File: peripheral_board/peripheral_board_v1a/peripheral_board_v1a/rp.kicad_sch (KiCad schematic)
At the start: 63 parts, among them CN1 Power Board Connector, CN2 DF11-16DP-2DSA(08), J1 Conn_01x03_Pin, J2 Conn_01x06, J3 Conn_02x06_Odd_Even, J4 Conn_01x06, J5 USB_C_Receptacle_USB2.0_16P, SW1 EVPAA602W, SW2 EVPAA602W, U1 RP2350A_C42411118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

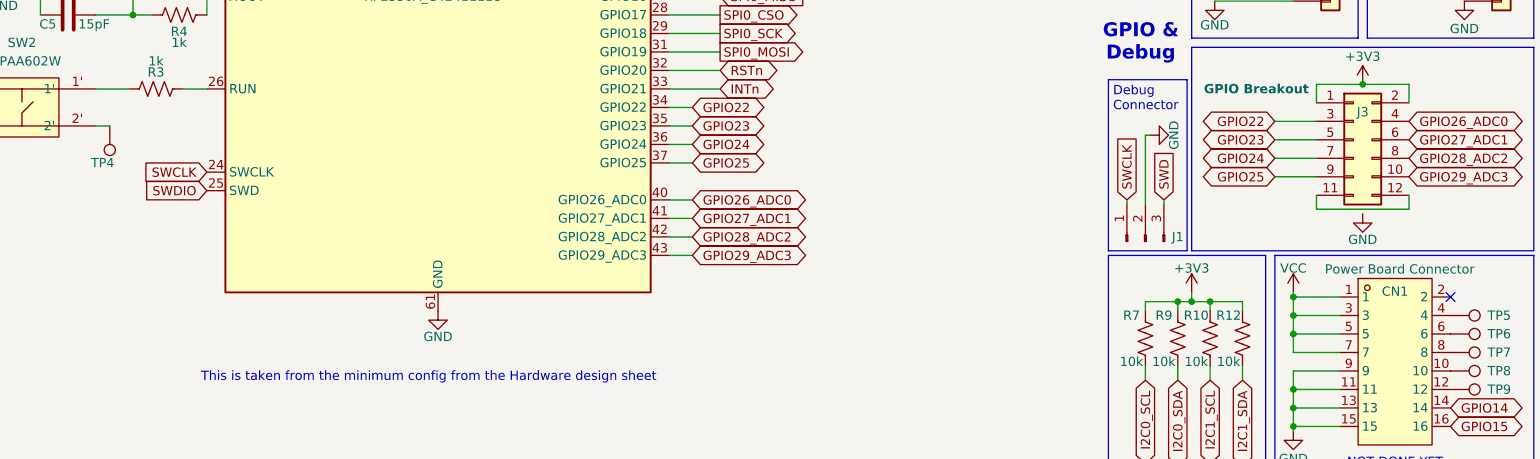
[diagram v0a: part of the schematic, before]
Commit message: PCB Update
Got all the parts on the board placed. Now just finishing the routing for each interconnection.
Trying to maintain a side to side/up to down but the board kinda follows it. For each plane  there is fill zones that will be for the chip that is on the top. Some of the traces are just being fed to where they need to go but the important EMI signals are being contained to their guidelines.
I will need to look at the lengths of the traces to make sure they are kept around the same length.

Will need to go over the board with some other eyes to make sure its ok.

I made sure the Wiznet traces are the same as SALAD.
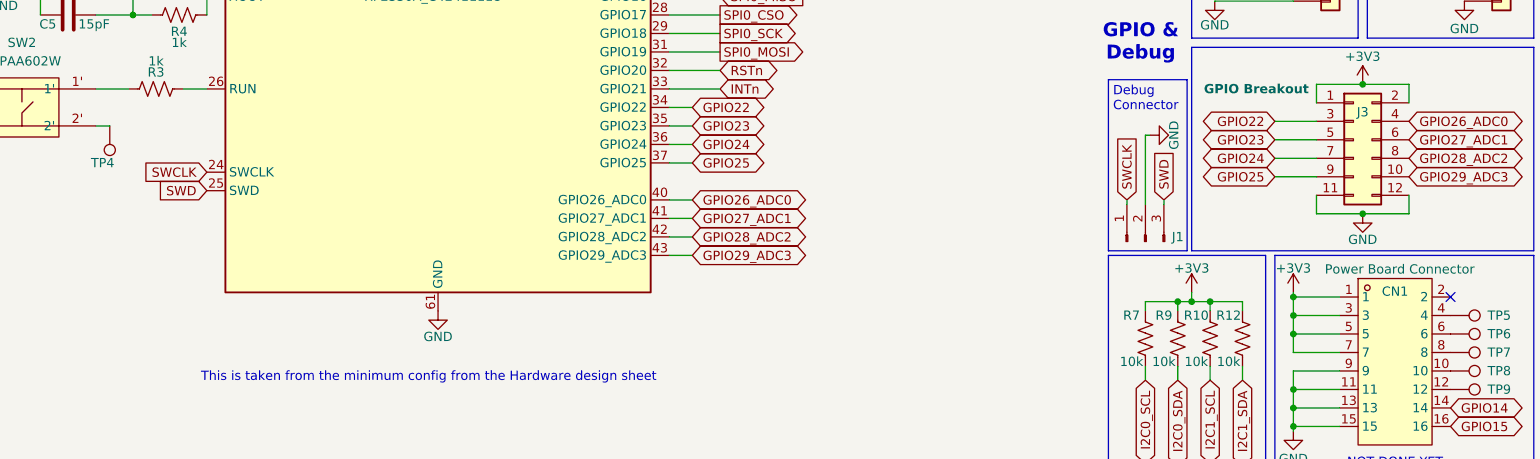
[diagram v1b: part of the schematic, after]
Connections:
- net SWDIO is gone; now on net SWD: U1.25 (SWD)
- net VCC is gone; now on net +3V3: CN1.1, CN1.3, CN1.5, CN1.7
- net GND: now also J3.11 (Pin_11), J3.12 (Pin_12)
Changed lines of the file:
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@@
 	)
 	(junction
+		(at 212.09 128.905)
+		(diameter 0)
+		(color 0 0 0 0)
+	)
+	(junction
 		(at 118.11 34.29)
 		(diameter 0)
@@
 	(wire
 		(pts
-			(xy 205.74 128.27) (xy 218.44 128.27)
+			(xy 205.74 128.905) (xy 212.09 128.905)
 		)
 		(stroke
@@
 	(wire
 		(pts
-			(xy 218.44 128.27) (xy 218.44 126.365)
+			(xy 218.44 128.905) (xy 218.44 126.365)
 		)
 		(stroke
@@
 	(wire
 		(pts
-			(xy 205.74 126.365) (xy 205.74 128.27)
+			(xy 205.74 126.365) (xy 205.74 128.905)
 		)
 		(stroke
@@
 	(wire
 		(pts
+			(xy 212.09 128.905) (xy 218.44 128.905)
+		)
+		(stroke
+			(width 0)
+			(type default)
+		)
+	)
+	(wire
+		(pts
 			(xy 123.19 76.2) (xy 116.84 76.2)
 		)
@@
 		)
 	)
-	(global_label "SWDIO"
+	(global_label "SWD"
 		(shape input)
 		(at 53.34 125.73 180)
@@
 		)
 		(property "Intersheetrefs" "${INTERSHEET_REFS}"
-			(at 44.4886 125.73 0)
+			(at 46.4239 125.73 0)
 			(effects
 				(font
@@
 			)
 		)
-		(property "Value" "VCC"
+		(property "Value" "+3V3"
 			(at 202.565 136.398 0)
 			(effects

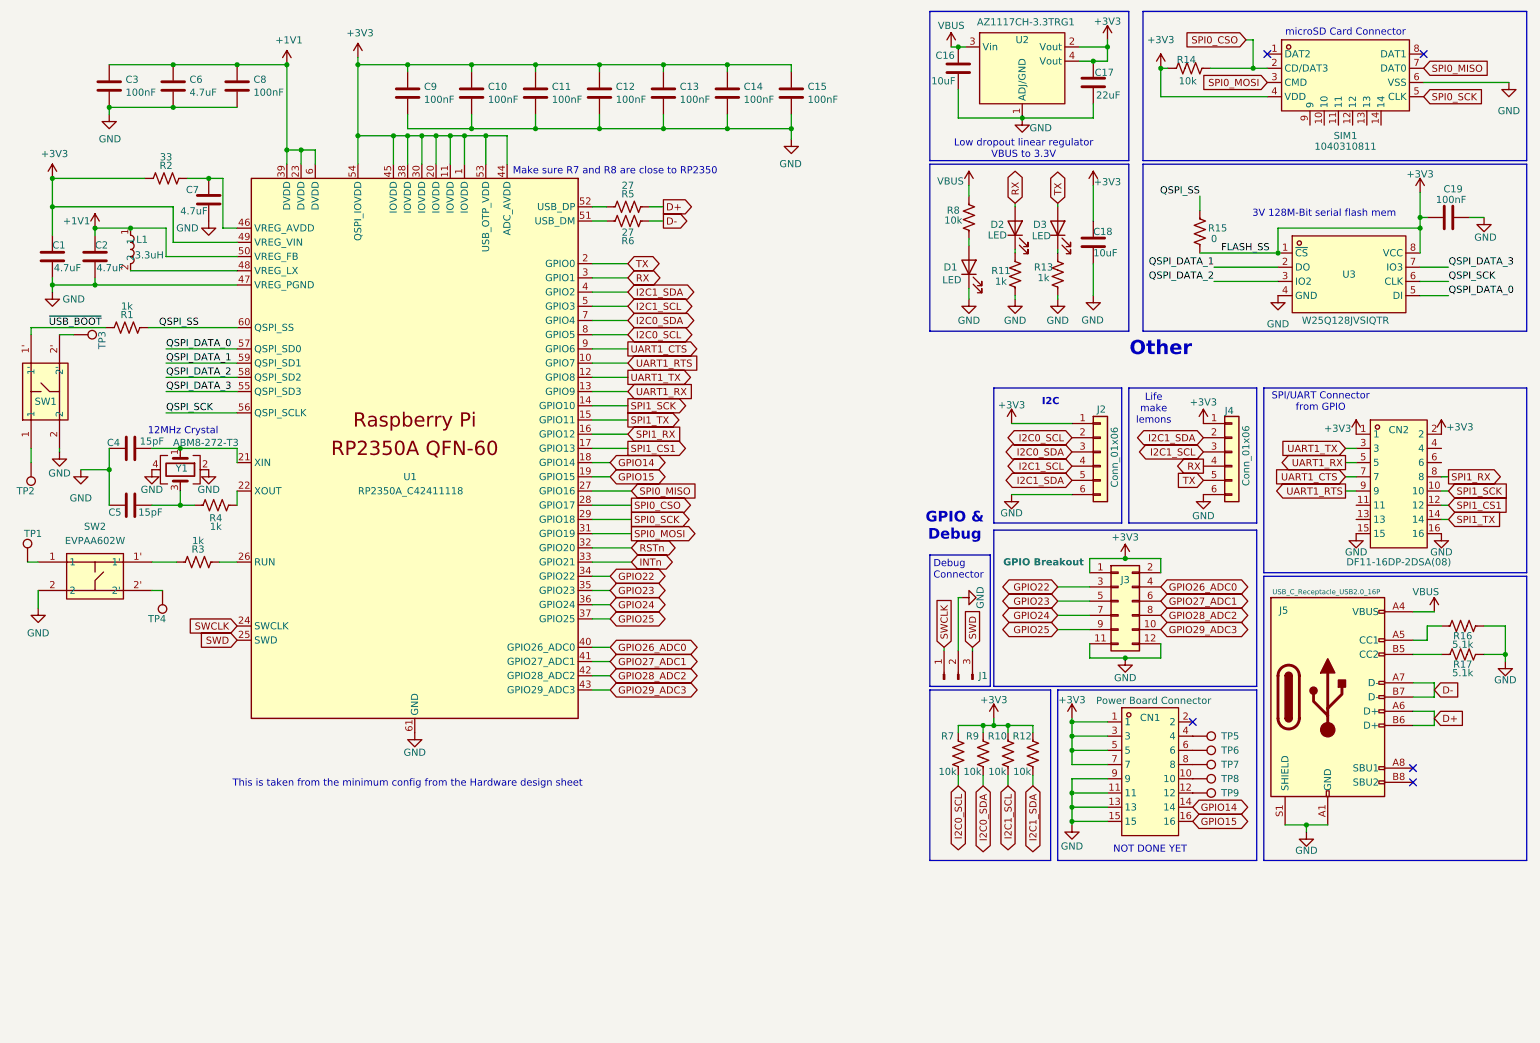
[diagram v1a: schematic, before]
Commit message: PCB almost done
Finished the routing except for the power board connector. Will be looking into adding in a Power path controller or similar. Want to add in via stitching for the DP signals. Should be just about done it would be more of just doing some change/improvements.
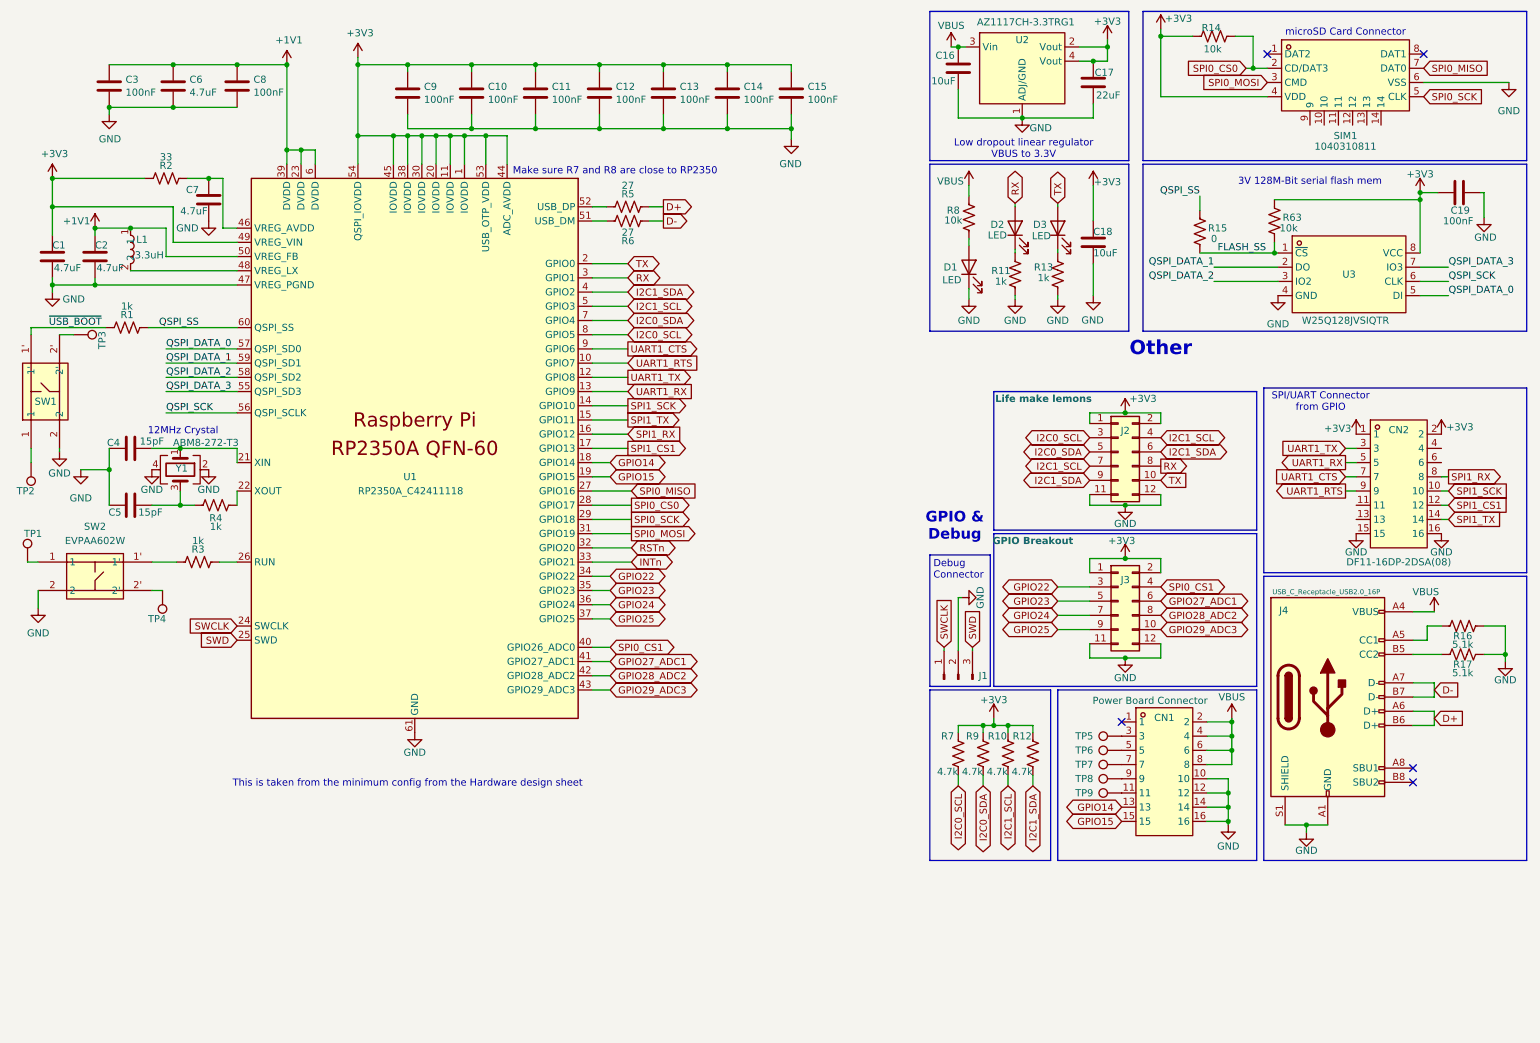
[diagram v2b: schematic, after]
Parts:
- removed J2, J4: Conn_01x06, SCALES:HDR-TH_6P-P2.54-V-M-1, symbol Connector_Generic:Conn_01x06
- added J2: Conn_02x06_Odd_Even, Connector_PinHeader_2.54mm:PinHeader_2x06_P2.54mm_Vertical, symbol Connector_Generic:Conn_02x06_Odd_Even
- added R63: 10k, Resistor_SMD:R_0402_1005Metric, symbol Device:R_US
- R10, R12, R7, R9: value 10k -> 4.7k
- R15: footprint Resistor_SMD:R_0603_1608Metric -> Resistor_SMD:R_0402_1005Metric
- SW1, SW2: footprint easyeda2kicad:KEY-TH_4P-L3.5-W4.9-P2.80-LS4.3 -> SCALES:KEY-TH_4P-L3.5-W4.9-P2.80-LS4.3
- renumbered J5 to J4
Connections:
- net +3V3: now also J2.1 (Pin_1), J2.2 (Pin_2), R63.1; no longer CN1.1, CN1.3, CN1.5, CN1.7, R15.2, U3.1 (~{CS})
- net GND: now also CN1.10, CN1.12, CN1.14, CN1.16, J2.11 (Pin_11), J2.12 (Pin_12); no longer CN1.11, CN1.13, CN1.15, CN1.9
- net GPIO14: now also CN1.13; no longer CN1.14
- net GPIO15: now also CN1.15; no longer CN1.16
- net I2C0_SCL: now also J2.3 (Pin_3)
- net I2C0_SDA: now also J2.5 (Pin_5)
- net I2C1_SCL: now also J2.4 (Pin_4), J2.7 (Pin_7)
- net I2C1_SDA: now also J2.6 (Pin_6), J2.9 (Pin_9)
- net RX: now also J2.8 (Pin_8)
- net TX: now also J2.10 (Pin_10)
- net VBUS: now also CN1.2, CN1.4, CN1.6, CN1.8
- net at TP9.1: now also CN1.11; no longer CN1.12
- net at TP8.1: now also CN1.9; no longer CN1.10
- net at TP7.1: now also CN1.7; no longer CN1.8
- net at TP5.1: now also CN1.3; no longer CN1.4
- net at TP6.1: now also CN1.5; no longer CN1.6
- net GPIO26_ADC0 renamed SPI0_CS1
- net SPI0_CSO renamed SPI0_CS0
- new net FLASH_SS: R15.2, R63.2, U3.1 (~{CS})
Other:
- note removed: "I2C"
- note removed: "Life make lemons"
- note removed: "NOT DONE YET"
- moved on the sheet: C19, CN1, R14, TP5, TP6, TP7, TP8, TP9

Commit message: PCB should be done
Finished the PCB just needs a review and then the part selection should be easy.
Added in stitching Vias.
Added in a Power controller for the two power sources of the USB or the external power board.
Removed the microSD card reader and added in XTSD which is just onboard NAND. It is around 1 gigabyte which should be enough space for any and all programs we are running.
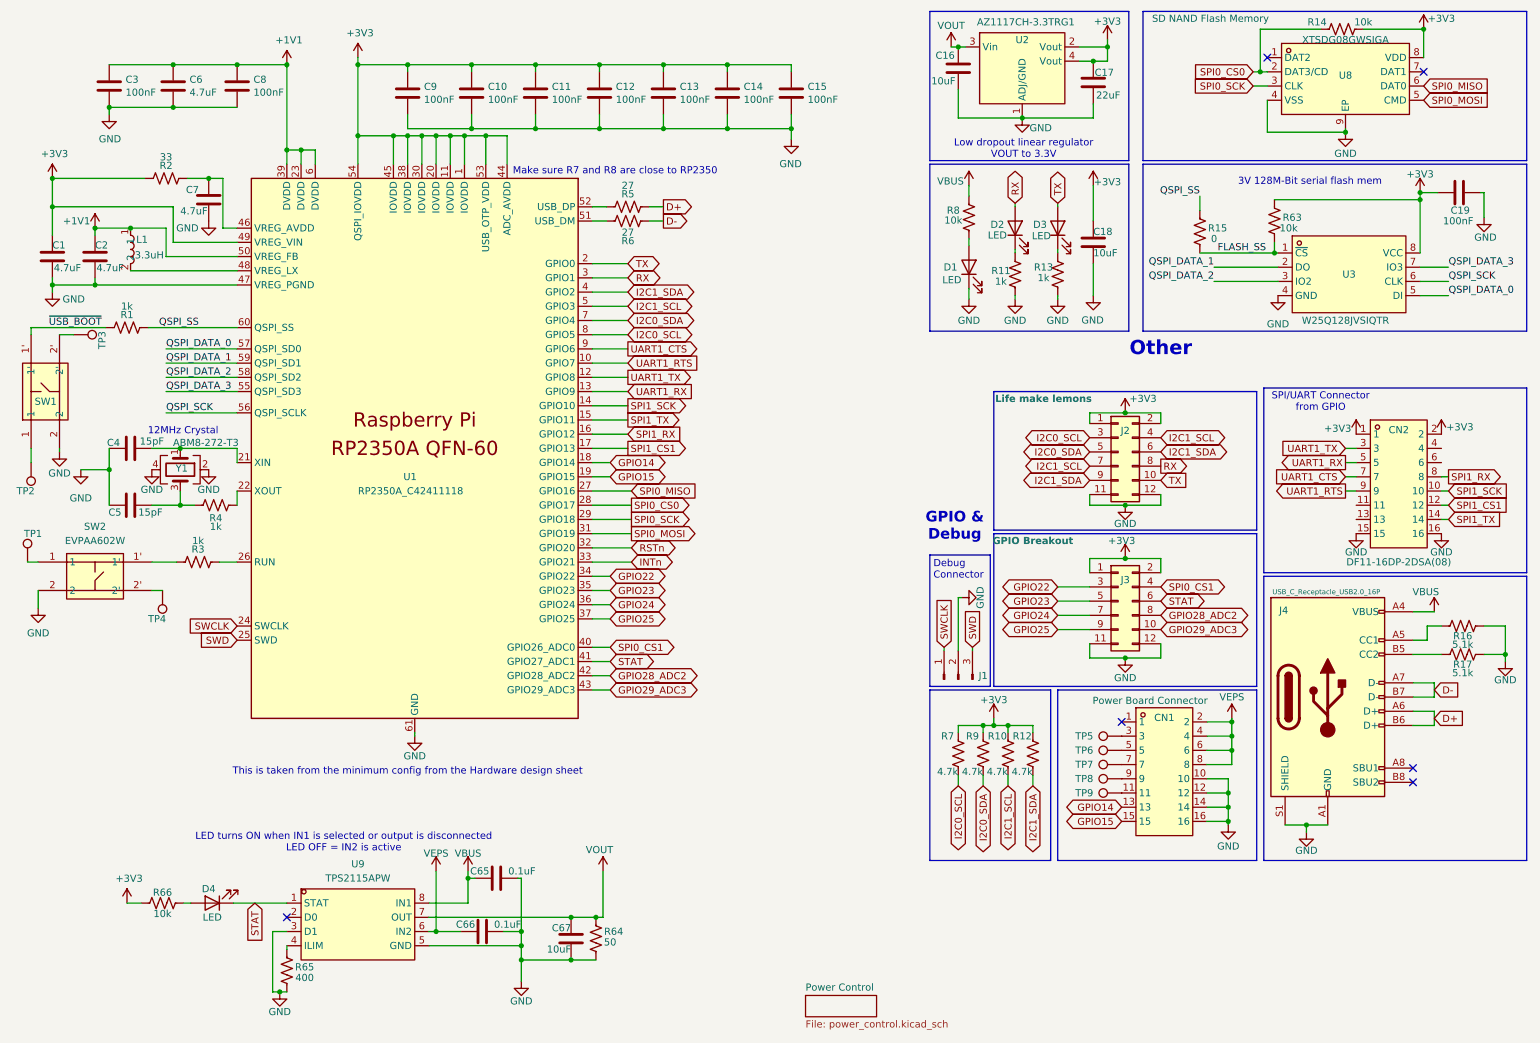
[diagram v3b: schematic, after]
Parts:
- removed SIM1: 1040310811, easyeda2kicad:SIM-SMD_8P-1040310811, symbol easyeda2kicad:1040310811
- added C65, C66: 0.1uF, Capacitor_SMD:C_0402_1005Metric, symbol Device:C
- added C67: 10uF, Capacitor_SMD:C_0402_1005Metric, symbol Device:C
- added D4: LED, LED_SMD:LED_0603_1608Metric, symbol Device:LED
- added R64: 50, Resistor_SMD:R_0603_1608Metric, symbol Device:R_US
- added R65: 400, Resistor_SMD:R_0603_1608Metric, symbol Device:R_US
- added R66: 10k, Resistor_SMD:R_0603_1608Metric, symbol Device:R_US
- added U8: XTSDG08GWSIGA, SCALES:W-PDFN-8_L8.0-W6.0-P1.27-BL-EP, symbol SCALES:XTSDG08GWSIGA
- added U9: TPS2115APW, SCALES:TSSOP-8_L4.4-W3.0-P0.65-LS6.4-BL, symbol SCALES:TPS2115APW
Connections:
- net +3V3: now also R14.1, R66.2, U8.8 (VDD); no longer R14.2
- net GND: now also C65.2, C66.2, C67.1, R64.1, R65.1, U8.4 (VSS), U8.9 (EP), U9.3 (D1), U9.5 (GND)
- net SPI0_CS0: now also R14.2, U8.2 (DAT3/CD); no longer R14.1
- net SPI0_MISO: now also U8.6 (DAT0)
- net SPI0_MOSI: now also U8.5 (CMD)
- net SPI0_SCK: now also U8.3 (CLK)
- net VBUS: now also C65.1, U9.8 (IN1); no longer C16.2, CN1.2, CN1.4, CN1.6, CN1.8, U2.3 (Vin)
- net GPIO27_ADC1 renamed STAT
- net STAT: now also D4.1 (K), U9.1 (STAT)
- new net: D4.2 (A), R66.1
- new net: R65.2, U9.4 (ILIM)
- new net VEPS: C66.1, CN1.2, CN1.4, CN1.6, CN1.8, U9.6 (IN2)
- new net VOUT: C16.2, C67.2, R64.2, U2.3 (Vin), U9.7 (OUT)
- no-connect marks 5 -> 6
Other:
- added sheet Power Control (power_control.kicad_sch)
- note added: "LED turns ON when IN1 is selected or output is disconnected LED OFF = IN2 is active"
- note added: "Low dropout linear regulator VOUT to 3.3V"
- note removed: "Low dropout linear regulator VBUS to 3.3V"
- note removed: "microSD Card Connector"
- moved on the sheet: R14

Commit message: Part picking for board
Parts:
- C65, C66: value 0.1uF -> 100nF
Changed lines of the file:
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@@
 			)
 		)
-		(property "Value" "0.1uF"
+		(property "Value" "100nF"
 			(at 104.14 176.53 90)
 			(effects
@@
 			)
 		)
-		(property "Value" "0.1uF"
+		(property "Value" "100nF"
 			(at 106.68 167.005 90)
 			(effects

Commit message: PCB step update
Made some additions to the 3d files for the project.
Deleted some old files that were just not being used.
Would like to restructure the folders and remove the v1 and make a folder that is just KiCad dependancies to help version control.
*Unsure if that is a good idea or if I should just leave it as project specific libriaries.*
Will look over this before this is merged to main.
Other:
- removed sheet Power Control
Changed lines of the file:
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@@
-		)
-	)
-	(sheet
-		(at 154.94 189.23)
-		(size 12.7 3.81)
-		(exclude_from_sim yes)
-		(in_bom no)
-		(on_board no)
-		(dnp yes)
-		(fields_autoplaced yes)
-		(stroke
-			(width 0.1524)
-			(type solid)
-		)
-		(fill
-			(color 0 0 0 0.0000)
-		)
-		(property "Sheetname" "Power Control"
-			(at 154.94 188.5184 0)
-			(effects
-				(font
-					(size 1.27 1.27)
-				)
-				(justify left bottom)
-			)
-		)
-		(property "Sheetfile" "power_control.kicad_sch"
-			(at 154.94 193.6246 0)
-			(effects
-				(font
-					(size 1.27 1.27)
-				)
-				(justify left top)
-			)
-		)
-		(instances
-			(project "peripheral_board_v1a"
-				(path "/14f8712f-1710-40cb-b01e-cc9b3c4405bd/3ab0c9bd-1966-49d5-9be4-af5813e74b9f"
-					(page "9")
-				)
-			)
 		)
 	)
